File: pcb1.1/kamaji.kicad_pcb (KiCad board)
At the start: 2 copper layers, 100 x 100 mm, 35 parts, among them J1 RJ10, J2 RJ10, J3 RJ10, J4 RJ10, Q1 IRF540N, SW1 CTRL1, SW2 CTRL2, SW3 CTRL3, U1 ATMEGA328P-PU, Y1 Crystal

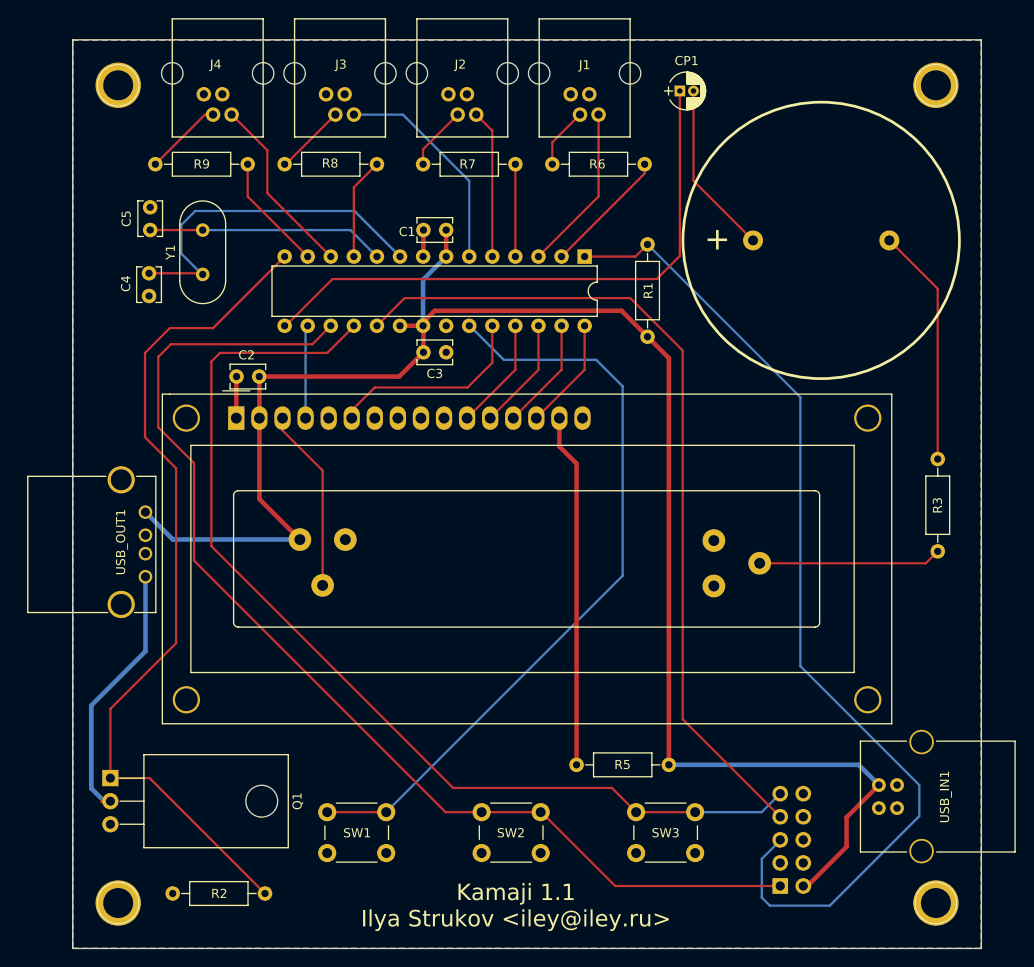
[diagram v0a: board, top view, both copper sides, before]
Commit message: pcb v1.1: re-route crystal, a few other adjustments
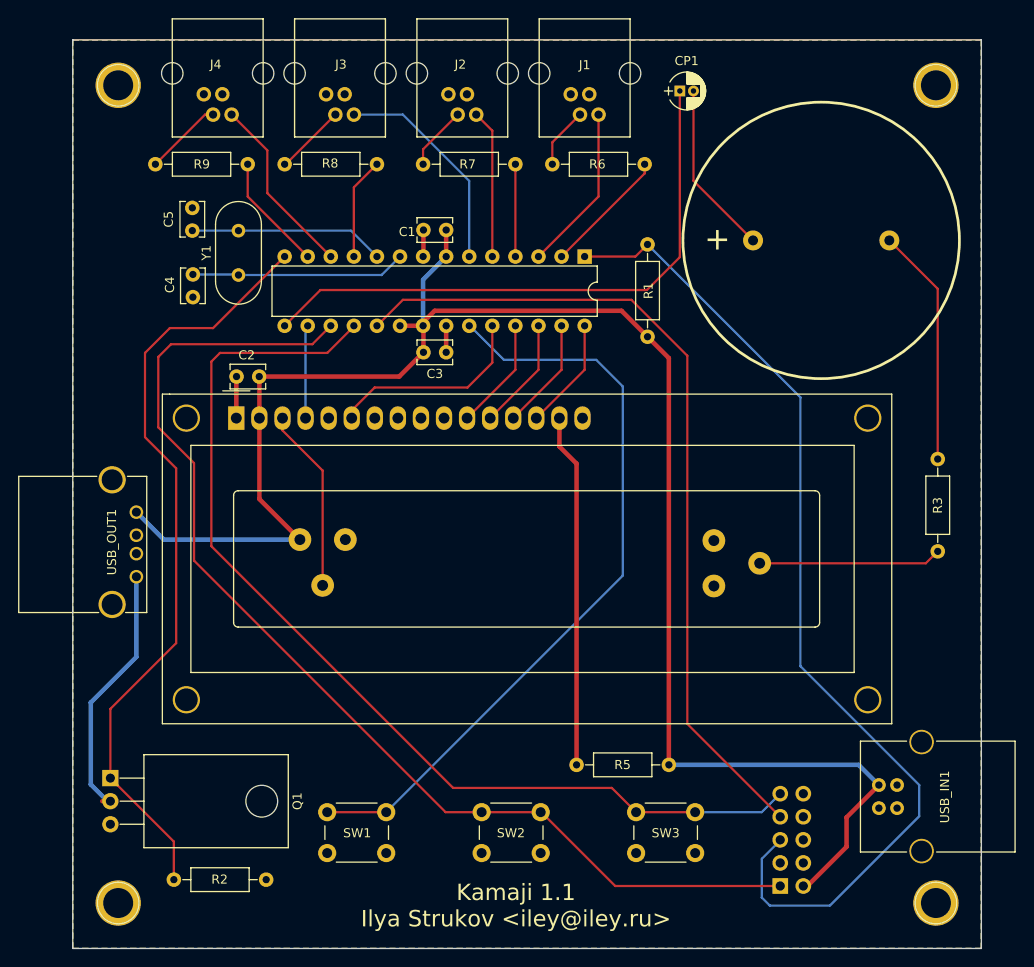
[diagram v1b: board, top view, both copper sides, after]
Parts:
- moved R2 10.1 mm to (111.1, 122.4), turned to 0 degrees
- moved C4 4.83 mm to (113.2, 55.8)
- moved C5 4.64 mm to (113.2, 51.0)
- moved Y1 3.94 mm to (118.2, 55.9)
- moved USB_OUT1 1.00 mm to (107.0, 82.0)
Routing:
- net XTAL1: track 39.2 -> 23.7 mm
- net LAMP: track 93.5 -> 85.3 mm
- net XTAL2: track 26.2 -> 21.5 mm
- net GND: track 7.52 -> 10.4 mm
- net VCC: track 188.3 -> 189.3 mm

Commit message: move the crystal and a usb socket
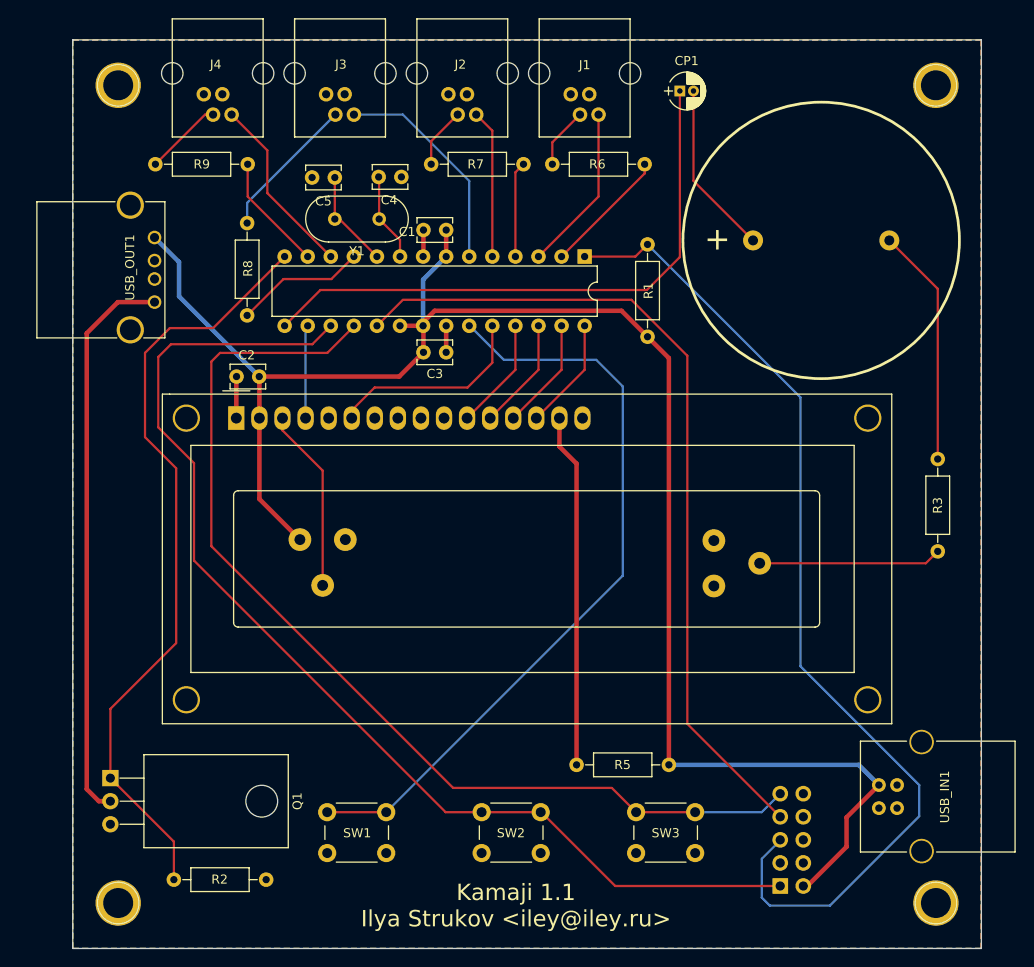
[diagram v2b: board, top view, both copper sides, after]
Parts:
- moved USB_OUT1 30.3 mm to (109.0, 51.8)
- moved C4 23.1 mm to (133.7, 45.1), turned to 0 degrees
- moved C5 16.7 mm to (128.8, 45.1), turned to 180 degrees
- moved Y1 16.7 mm to (133.7, 49.7), turned to 180 degrees
- moved R8 7.68 mm to (119.2, 50.2), turned to 270 degrees
- moved R7 0.89 mm to (139.4, 43.7)
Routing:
- net Net-(Q1-Pad2): track 29.8 -> 64.5 mm
- net XTAL1: track 23.7 -> 9.74 mm
- net XTAL2: track 21.5 -> 10.9 mm
- net Net-(J3-Pad2): track 7.85 -> 16.0 mm
- net PLED3: track 11.2 -> 14.4 mm
- net VCC: track 189.3 -> 190.1 mm
